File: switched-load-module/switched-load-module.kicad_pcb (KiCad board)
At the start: 2 copper layers, 60 x 55 mm, 38 parts, among them J1 Conn_01x03, J2 Screw_Terminal_01x04, J3 Conn_01x03, J4 Screw_Terminal_01x05, Q1 BCW66H, Q2 Q_NMOS_GDS, U1 PC817, U2 L78L05_SOT89, U3 HFBR-2521Z, U4 DGD0211C

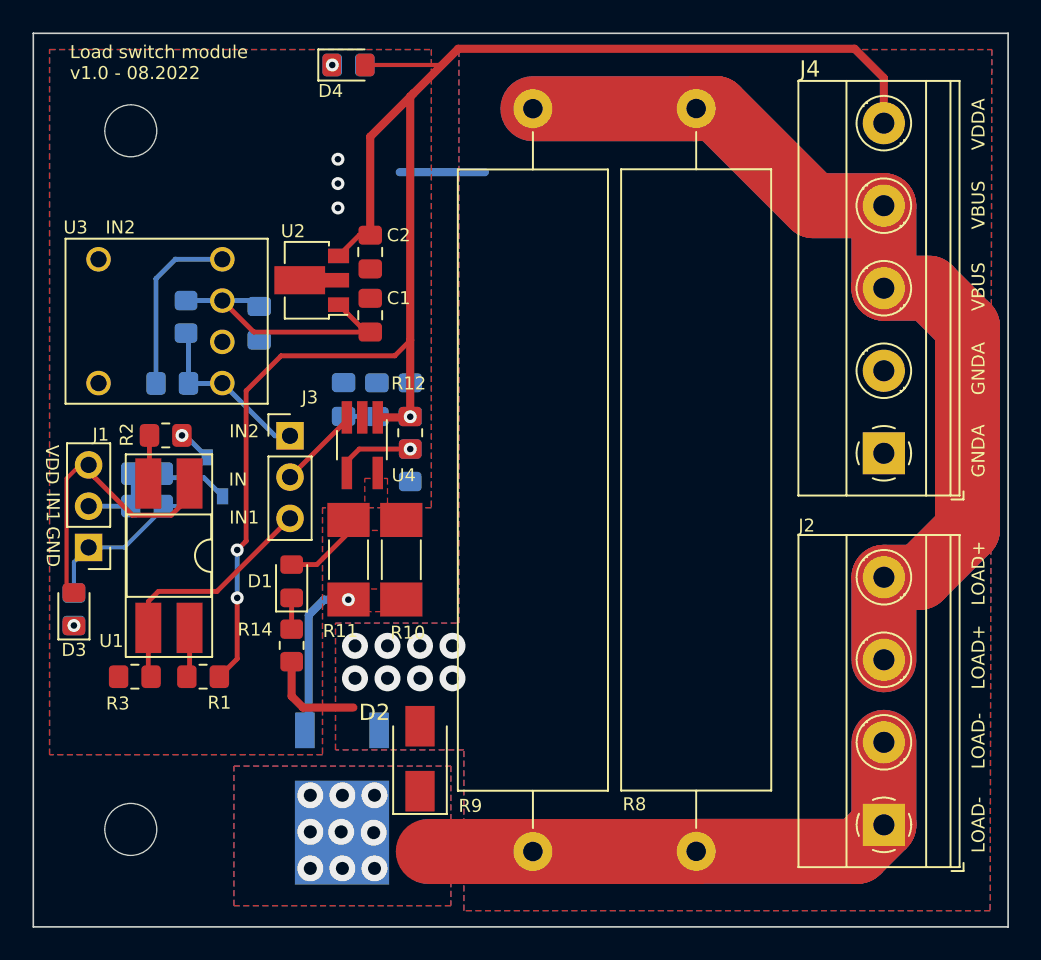
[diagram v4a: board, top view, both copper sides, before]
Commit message: Adjusted clearence for low-side switch module
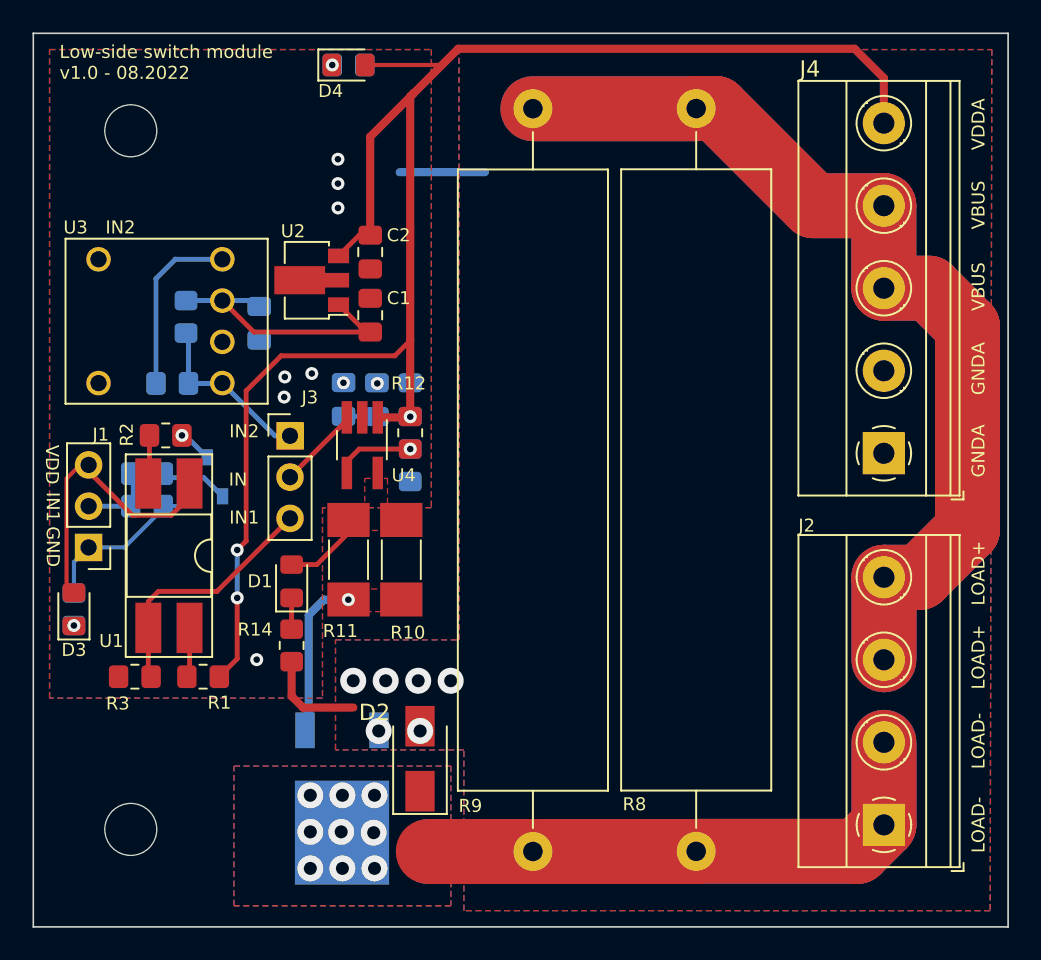
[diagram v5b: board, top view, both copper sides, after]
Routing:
- net GNDA: vias 11 -> 15
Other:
- board text added: "Low-side switch module v1.0 - 08.2022"
- board text removed: "Load switch module v1.0 - 08.2022"
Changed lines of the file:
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@@
     (effects (font (size 0.8 0.8) (thickness 0.2)))
   )
-  (gr_text "Load switch module\nv1.0 - 08.2022" (at 40.6 46.05) (layer "F.SilkS")
+  (gr_text "Low-side switch module\nv1.0 - 08.2022" (at 39.96 46.04) (layer "F.SilkS")
     (effects (font (size 0.8 0.8) (thickness 0.2)) (justify left))
   )
@@
   (segment (start 54.95 85.75) (end 58.05 85.75) (width 0.5) (layer "F.Cu") (net 1))
   (via (at 57.1 55) (size 0.8) (drill 0.4) (layers "F.Cu" "B.Cu") (free) (net 1))
-  (via (at 58.15 81.95) (size 1.6) (drill 0.8) (layers "F.Cu" "B.Cu") (free) (net 1))
+  (via (at 59.52 65.8) (size 0.8) (drill 0.4) (layers "F.Cu" "B.Cu") (net 1))
+  (via (at 53.83 65.4) (size 0.8) (drill 0.4) (layers "F.Cu" "B.Cu") (free) (net 1))
+  (via (at 58.04 84.1) (size 1.6) (drill 0.8) (layers "F.Cu" "B.Cu") (free) (net 1))
   (via (at 57.1 52) (size 0.8) (drill 0.4) (layers "F.Cu" "B.Cu") (free) (net 1))
-  (via (at 64.15 81.95) (size 1.6) (drill 0.8) (layers "F.Cu" "B.Cu") (free) (net 1))
-  (via (at 60.15 83.95) (size 1.6) (drill 0.8) (layers "F.Cu" "B.Cu") (free) (net 1))
-  (via (at 62.15 83.95) (size 1.6) (drill 0.8) (layers "F.Cu" "B.Cu") (free) (net 1))
-  (via (at 64.15 83.95) (size 1.6) (drill 0.8) (layers "F.Cu" "B.Cu") (free) (net 1))
-  (via (at 62.15 81.95) (size 1.6) (drill 0.8) (layers "F.Cu" "B.Cu") (free) (net 1))
+  (via (at 64.04 84.1) (size 1.6) (drill 0.8) (layers "F.Cu" "B.Cu") (free) (net 1))
+  (via (at 62.16 87.19) (size 1.6) (drill 0.8) (layers "F.Cu" "B.Cu") (free) (net 1))
+  (via (at 55.49 65.19) (size 0.8) (drill 0.4) (layers "F.Cu" "B.Cu") (free) (net 1))
+  (via (at 52.1 82.8) (size 0.8) (drill 0.4) (layers "F.Cu" "B.Cu") (free) (net 1))
+  (via (at 53.79 66.64) (size 0.8) (drill 0.4) (layers "F.Cu" "B.Cu") (free) (net 1))
+  (via (at 62.04 84.1) (size 1.6) (drill 0.8) (layers "F.Cu" "B.Cu") (free) (net 1))
   (via (at 57.1 53.5) (size 0.8) (drill 0.4) (layers "F.Cu" "B.Cu") (free) (net 1))
-  (via (at 60.15 81.95) (size 1.6) (drill 0.8) (layers "F.Cu" "B.Cu") (free) (net 1))
-  (via (at 58.15 83.95) (size 1.6) (drill 0.8) (layers "F.Cu" "B.Cu") (free) (net 1))
+  (via (at 60.04 84.1) (size 1.6) (drill 0.8) (layers "F.Cu" "B.Cu") (free) (net 1))
+  (via (at 59.61 87.19) (size 1.6) (drill 0.8) (layers "F.Cu" "B.Cu") (free) (net 1))
+  (via (at 57.44 65.76) (size 0.8) (drill 0.4) (layers "F.Cu" "B.Cu") (net 1))
   (segment (start 60.9 52.8) (end 66.15 52.8) (width 0.5) (layer "B.Cu") (net 1))
   (segment (start 59.0875 62.6375) (end 51.9215 62.6375) (width 0.3) (layer "F.Cu") (net 2))
@@
   (zone (net 1) (net_name "GNDA") (layers F&B.Cu) (hatch edge 0.508)
     (priority 1)
-    (connect_pads thru_hole_only (clearance 0.254))
+    (connect_pads thru_hole_only (clearance 1))
     (min_thickness 0.254) (filled_areas_thickness no)
     (fill yes (thermal_gap 0.254) (thermal_bridge_width 1.25))
@@
         (xy 64.85 88.35)
         (xy 56.95 88.35)
-        (xy 56.95 80.55)
-        (xy 64.55 80.55)
+        (xy 56.95 81.58)
+        (xy 64.55 81.58)
         (xy 64.55 45.25)
         (xy 97.346223 45.251881)
@@
         (xy 62.85 73.45)
         (xy 56.15 73.45)
-        (xy 56.15 88.65)
-        (xy 39.35 88.65)
+        (xy 56.15 85.17)
+        (xy 39.35 85.17)
         (xy 39.35 45.25)
         (xy 62.85 45.25)
